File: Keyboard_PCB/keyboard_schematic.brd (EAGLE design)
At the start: 460 x 121 mm, 230 parts

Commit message: Updated Schematic
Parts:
- removed 0, 1, 2, 3, 4, 5, 6, 7, 8, 9, A, ALT, ALT2, B, BACKSLASH, BACKSONG, BACKSPACE_1, C, CAPSLOCK, COMMA, CTRL, CTRL2, D, DASH, DELETE, DELETE2, DOWN, E, END, ENTER2, EQUAL, EQUAL2, ESC, F, F1, F10, F11, F12, F2, F3, F4, F5, F6, F7, F8, F9, G, GRAVE, H, HOME, I, INSERT, J, K, KP_1, KP_2, KP_3, KP_4, KP_5, KP_52, KP_6, KP_62, KP_7, KP_8, KP_9, KP_ASTERISK, KP_DASH, KP_DEL, KP_SLASH, L, LBRACKET, LEFT, M, MENU, N, NEXTSONG, NUMLOCK, O, P, PAUSE, PAUSEPLAY, PERIOD, PGDN, PGUP, PRTSC, Q, QUOTE, R, RANDSONG, RBRACKET, RIGHT, S, SCROLLLOCK, SEMICOLON, SLASH, T, TAB, U, UNDERSCORE, UP, V, VOLUMEUP, VOLUMNEDOWN, W, WIN, WIN2, X, Y, Z: KEYSWITCH-RGBLED-MX-1U-RGB, Keyboard:MX-1U-RGB
- removed BACKSPACE, ENTER, KP_0, SHIFT, SHIFT2: KEYSWITCH-RGBLED-MX-2U-RGB, Keyboard:MX-2U-RGB
- removed D0, D1, D2, D3, D4, D5, D6, D7, D8, D9, DA, DALT, DALT2, DB, DBACKSLASH, DBACKSONG, DBACKSPACE, DBACKSPACE_1, DC, DCAPSLOCK, DCOMMA, DCTRL, DCTRL2, DD, DDASH, DDELETE, DDELETE2, DDOWN, DE, DEND, DENTER, DENTER2, DEQUAL, DEQUAL2, DESC, DF, DF1, DF10, DF11, DF12, DF2, DF3, DF4, DF5, DF6, DF7, DF8, DF9, DG, DGRAVE, DH, DHOME, DI, DINSERT, DJ, DK, DKP_0, DKP_1, DKP_2, DKP_3, DKP_4, DKP_5, DKP_52, DKP_6, DKP_62, DKP_7, DKP_8, DKP_9, DKP_ASTERISK, DKP_DASH, DKP_DEL, DKP_SLASH, DL, DLBRACKET, DLEFT, DM, DMENU, DN, DNEXTSONG, DNUMLOCK, DO, DP, DPAUSE, DPAUSEPLAY, DPERIOD, DPGDN, DPGUP, DPRTSC, DQ, DQUOTE, DR, DRANDSONG, DRBRACKET, DRIGHT, DS, DSCROLLLOCK, DSEMICOLON, DSHIFT, DSHIFT2, DSLASH, DSPACE, DT, DTAB, DU, DUNDERSCORE, DUP, DV, DVOLUMEUP, DVOLUMNEDOWN, DW, DWIN, DWIN2, DX, DY, DZ: 1N4148, Components:DO-35
- removed SPACE: KEYSWITCH-RGBLED-MX-6.25U-RGB, Keyboard:MX-6.25U-RGB
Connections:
- removed net ROW1.5: DBACKSONG.C, DESC.C, DF1.C, DF10.C, DF11.C, DF12.C, DF2.C, DF3.C, DF4.C, DF5.C, DF6.C, DF7.C, DF8.C, DF9.C, DNEXTSONG.C, DPAUSE.C, DPAUSEPLAY.C, DPRTSC.C, DRANDSONG.C, DSCROLLLOCK.C, DVOLUMEUP.C, DVOLUMNEDOWN.C
- removed net ROW2.5: D0.C, D1.C, D2.C, D3.C, D4.C, D5.C, D6.C, D7.C, D8.C, D9.C, DBACKSPACE.C, DDASH.C, DEQUAL.C, DGRAVE.C, DHOME.C, DINSERT.C, DKP_ASTERISK.C, DKP_DASH.C, DKP_SLASH.C, DNUMLOCK.C, DPGUP.C, DUNDERSCORE.C
- removed net ROW3.5: DBACKSLASH.C, DDELETE.C, DE.C, DEND.C, DI.C, DKP_7.C, DKP_8.C, DKP_9.C, DLBRACKET.C, DO.C, DP.C, DPGDN.C, DQ.C, DR.C, DRBRACKET.C, DT.C, DTAB.C, DU.C, DW.C, DY.C
- removed net ROW4.5: DA.C, DCAPSLOCK.C, DD.C, DENTER.C, DF.C, DG.C, DH.C, DJ.C, DK.C, DKP_4.C, DKP_52.C, DKP_6.C, DKP_62.C, DL.C, DQUOTE.C, DS.C, DSEMICOLON.C
- removed net ROW5.5: DB.C, DC.C, DCOMMA.C, DKP_1.C, DKP_2.C, DKP_3.C, DM.C, DN.C, DPERIOD.C, DSHIFT.C, DSHIFT2.C, DSLASH.C, DUP.C, DV.C, DX.C, DZ.C
- removed net ROW6.5: DALT.C, DALT2.C, DBACKSPACE_1.C, DCTRL.C, DCTRL2.C, DDOWN.C, DKP_0.C, DKP_DEL.C, DLEFT.C, DMENU.C, DRIGHT.C, DSPACE.C, DWIN.C, DWIN2.C

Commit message: Final Revision on positioning
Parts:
- added 0, 1, 2, 3, 4, 5, 6, 7, 8, 9, A, ALT, ALT2, B, BACKSLASH, BACKSONG, BACKSPACE_1, C, CAPSLOCK, COMMA, CTRL, CTRL2, D, DASH, DELETE, DELETE2, DOWN, E, END, ENTER2, EQUAL, EQUAL2, ESC, F, F1, F10, F11, F12, F2, F3, F4, F5, F6, F7, F8, F9, G, GRAVE, H, HOME, I, INSERT, J, K, KP_1, KP_2, KP_3, KP_4, KP_5, KP_52, KP_6, KP_62, KP_7, KP_8, KP_9, KP_ASTERISK, KP_DASH, KP_DEL, KP_SLASH, L, LBRACKET, LEFT, M, MENU, N, NEXTSONG, NUMLOCK, O, P, PAUSE, PAUSEPLAY, PERIOD, PGDN, PGUP, PRTSC, Q, QUOTE, R, RANDSONG, RBRACKET, RIGHT, S, SCROLLLOCK, SEMICOLON, SLASH, T, TAB, U, UNDERSCORE, UP, V, VOLUMEUP, VOLUMNEDOWN, W, WIN, WIN2, X, Y, Z: KEYSWITCH-RGBSMDLED-ALPSMX-1U-SMDRGB, Keyboard:ALPSMX-1U-SMDRGB
- added BACKSPACE, ENTER, KP_0, SHIFT, SHIFT2: KEYSWITCH-RGBSMDLED-ALPSMX-2U-SMDRGB, Keyboard:ALPSMX-2U-SMDRGB
- added D0, D1, D2, D3, D4, D5, D6, D7, D8, D9, DA, DALT, DALT2, DB, DBACKSLASH, DBACKSONG, DBACKSPACE, DBACKSPACE_1, DC, DCAPSLOCK, DCOMMA, DCTRL, DCTRL2, DD, DDASH, DDELETE, DDELETE2, DDOWN, DE, DEND, DENTER, DENTER2, DEQUAL, DEQUAL2, DESC, DF, DF1, DF10, DF11, DF12, DF2, DF3, DF4, DF5, DF6, DF7, DF8, DF9, DG, DGRAVE, DH, DHOME, DI, DINSERT, DJ, DK, DKP_0, DKP_1, DKP_2, DKP_3, DKP_4, DKP_5, DKP_52, DKP_6, DKP_62, DKP_7, DKP_8, DKP_9, DKP_ASTERISK, DKP_DASH, DKP_DEL, DKP_SLASH, DL, DLBRACKET, DLEFT, DM, DMENU, DN, DNEXTSONG, DNUMLOCK, DO, DP, DPAUSE, DPAUSEPLAY, DPERIOD, DPGDN, DPGUP, DPRTSC, DQ, DQUOTE, DR, DRANDSONG, DRBRACKET, DRIGHT, DS, DSCROLLLOCK, DSEMICOLON, DSHIFT, DSHIFT2, DSLASH, DSPACE, DT, DTAB, DU, DUNDERSCORE, DUP, DV, DVOLUMEUP, DVOLUMNEDOWN, DW, DWIN, DWIN2, DX, DY, DZ: (no value), Components:SOD-123
- added SPACE: KEYSWITCH-RGBSMDLED-ALPSMX-6.25U-SMDRGB, Keyboard:ALPSMX-6.25U-SMDRGB
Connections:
- new net N$1: DESC.A, ESC.ALPS2, ESC.MX2
- new net N$10: DF9.A, F9.ALPS2, F9.MX2
- new net N$100: DENTER2.A, ENTER2.ALPS2, ENTER2.MX2
- new net N$101: DDELETE2.A, DELETE2.ALPS2, DELETE2.MX2
- new net N$102: CTRL.ALPS2, CTRL.MX2, DCTRL.A
- new net N$103: DWIN.A, WIN.ALPS2, WIN.MX2
- new net N$104: ALT.ALPS2, ALT.MX2, DALT.A
- new net N$105: DSPACE.A, SPACE.ALPS2, SPACE.MX2
- new net N$106: ALT2.ALPS2, ALT2.MX2, DALT2.A
- new net N$107: DWIN2.A, WIN2.ALPS2, WIN2.MX2
- new net N$108: DMENU.A, MENU.ALPS2, MENU.MX2
- new net N$109: CTRL2.ALPS2, CTRL2.MX2, DCTRL2.A
- new net N$11: DF10.A, F10.ALPS2, F10.MX2
- new net N$110: DLEFT.A, LEFT.ALPS2, LEFT.MX2
- new net N$111: DDOWN.A, DOWN.ALPS2, DOWN.MX2
- new net N$112: DRIGHT.A, RIGHT.ALPS2, RIGHT.MX2
- new net N$113: DKP_0.A, KP_0.ALPS2, KP_0.MX2
- new net N$114: DKP_DEL.A, KP_DEL.ALPS2, KP_DEL.MX2
- new net N$115: BACKSPACE_1.ALPS2, BACKSPACE_1.MX2, DBACKSPACE_1.A
- new net N$12: DF11.A, F11.ALPS2, F11.MX2
- new net N$13: DF12.A, F12.ALPS2, F12.MX2
- new net N$14: DVOLUMEUP.A, VOLUMEUP.ALPS2, VOLUMEUP.MX2
- new net N$15: DVOLUMNEDOWN.A, VOLUMNEDOWN.ALPS2, VOLUMNEDOWN.MX2
- new net N$16: DPRTSC.A, PRTSC.ALPS2, PRTSC.MX2
- new net N$17: DSCROLLLOCK.A, SCROLLLOCK.ALPS2, SCROLLLOCK.MX2
- new net N$18: DPAUSE.A, PAUSE.ALPS2, PAUSE.MX2
- new net N$19: BACKSONG.ALPS2, BACKSONG.MX2, DBACKSONG.A
- new net N$2: DF1.A, F1.ALPS2, F1.MX2
- new net N$20: DPAUSEPLAY.A, PAUSEPLAY.ALPS2, PAUSEPLAY.MX2
- new net N$21: DNEXTSONG.A, NEXTSONG.ALPS2, NEXTSONG.MX2
- new net N$22: DRANDSONG.A, RANDSONG.ALPS2, RANDSONG.MX2
- new net N$23: DGRAVE.A, GRAVE.ALPS2, GRAVE.MX2
- new net N$24: 1.ALPS2, 1.MX2, D1.A
- new net N$25: 2.ALPS2, 2.MX2, D2.A
- new net N$26: 3.ALPS2, 3.MX2, D3.A
- new net N$27: 4.ALPS2, 4.MX2, D4.A
- new net N$28: 5.ALPS2, 5.MX2, D5.A
- new net N$29: 6.ALPS2, 6.MX2, D6.A
- new net N$3: DF2.A, F2.ALPS2, F2.MX2
- new net N$30: 7.ALPS2, 7.MX2, D7.A
- new net N$31: 8.ALPS2, 8.MX2, D8.A
- new net N$32: 9.ALPS2, 9.MX2, D9.A
- new net N$33: 0.ALPS2, 0.MX2, D0.A
- new net N$34: DASH.ALPS2, DASH.MX2, DDASH.A
- new net N$35: DEQUAL.A, EQUAL.ALPS2, EQUAL.MX2
- new net N$36: BACKSPACE.ALPS2, BACKSPACE.MX2, DBACKSPACE.A
- new net N$37: DINSERT.A, INSERT.ALPS2, INSERT.MX2
- new net N$38: DHOME.A, HOME.ALPS2, HOME.MX2
- new net N$39: DPGUP.A, PGUP.ALPS2, PGUP.MX2
- new net N$4: DF3.A, F3.ALPS2, F3.MX2
- new net N$40: DNUMLOCK.A, NUMLOCK.ALPS2, NUMLOCK.MX2
- new net N$41: DKP_SLASH.A, KP_SLASH.ALPS2, KP_SLASH.MX2
- new net N$42: DKP_ASTERISK.A, KP_ASTERISK.ALPS2, KP_ASTERISK.MX2
- new net N$43: DKP_DASH.A, KP_DASH.ALPS2, KP_DASH.MX2
- new net N$44: DUNDERSCORE.A, UNDERSCORE.ALPS2, UNDERSCORE.MX2
- new net N$45: DTAB.A, TAB.ALPS2, TAB.MX2
- new net N$46: DQ.A, Q.ALPS2, Q.MX2
- new net N$47: DW.A, W.ALPS2, W.MX2
- new net N$48: DE.A, E.ALPS2, E.MX2
- new net N$49: DR.A, R.ALPS2, R.MX2
- new net N$5: DF4.A, F4.ALPS2, F4.MX2
- new net N$50: DT.A, T.ALPS2, T.MX2
- new net N$51: DY.A, Y.ALPS2, Y.MX2
- new net N$52: DU.A, U.ALPS2, U.MX2
- new net N$53: DI.A, I.ALPS2, I.MX2
- new net N$54: DO.A, O.ALPS2, O.MX2
- new net N$55: DP.A, P.ALPS2, P.MX2
- new net N$56: DLBRACKET.A, LBRACKET.ALPS2, LBRACKET.MX2
- new net N$57: DRBRACKET.A, RBRACKET.ALPS2, RBRACKET.MX2
- new net N$58: BACKSLASH.ALPS2, BACKSLASH.MX2, DBACKSLASH.A
- new net N$59: DDELETE.A, DELETE.ALPS2, DELETE.MX2
- new net N$6: DF5.A, F5.ALPS2, F5.MX2
- new net N$60: DEND.A, END.ALPS2, END.MX2
- new net N$61: DPGDN.A, PGDN.ALPS2, PGDN.MX2
- new net N$62: DKP_7.A, KP_7.ALPS2, KP_7.MX2
- new net N$63: DKP_8.A, KP_8.ALPS2, KP_8.MX2
- new net N$64: DKP_9.A, KP_9.ALPS2, KP_9.MX2
- new net N$65: DEQUAL2.A, EQUAL2.ALPS2, EQUAL2.MX2
- new net N$66: DKP_5.A, KP_5.ALPS2, KP_5.MX2
- new net N$67: CAPSLOCK.ALPS2, CAPSLOCK.MX2, DCAPSLOCK.A
- new net N$68: A.ALPS2, A.MX2, DA.A
- new net N$69: DS.A, S.ALPS2, S.MX2
- new net N$7: DF6.A, F6.ALPS2, F6.MX2
- new net N$70: D.ALPS2, D.MX2, DD.A
- new net N$71: DF.A, F.ALPS2, F.MX2
- new net N$72: DG.A, G.ALPS2, G.MX2
- new net N$73: DH.A, H.ALPS2, H.MX2
- new net N$74: DJ.A, J.ALPS2, J.MX2
- new net N$75: DK.A, K.ALPS2, K.MX2
- new net N$76: DL.A, L.ALPS2, L.MX2
- new net N$77: DSEMICOLON.A, SEMICOLON.ALPS2, SEMICOLON.MX2
- new net N$78: DQUOTE.A, QUOTE.ALPS2, QUOTE.MX2
- new net N$79: DENTER.A, ENTER.ALPS2, ENTER.MX2
- new net N$8: DF7.A, F7.ALPS2, F7.MX2
- new net N$80: DKP_4.A, KP_4.ALPS2, KP_4.MX2
- new net N$81: DKP_52.A, KP_52.ALPS2, KP_52.MX2
- new net N$82: DKP_6.A, KP_6.ALPS2, KP_6.MX2
- new net N$83: DKP_62.A, KP_62.ALPS2, KP_62.MX2
- new net N$84: DSHIFT.A, SHIFT.ALPS2, SHIFT.MX2
- new net N$85: DZ.A, Z.ALPS2, Z.MX2
- new net N$86: DX.A, X.ALPS2, X.MX2
- new net N$87: C.ALPS2, C.MX2, DC.A
- new net N$88: DV.A, V.ALPS2, V.MX2
- new net N$89: B.ALPS2, B.MX2, DB.A
- new net N$9: DF8.A, F8.ALPS2, F8.MX2
- new net N$90: DN.A, N.ALPS2, N.MX2
- new net N$91: DM.A, M.ALPS2, M.MX2
- new net N$92: COMMA.ALPS2, COMMA.MX2, DCOMMA.A
- new net N$93: DPERIOD.A, PERIOD.ALPS2, PERIOD.MX2
- new net N$94: DSLASH.A, SLASH.ALPS2, SLASH.MX2
- new net N$95: DSHIFT2.A, SHIFT2.ALPS2, SHIFT2.MX2
- new net N$96: DUP.A, UP.ALPS2, UP.MX2
- new net N$97: DKP_1.A, KP_1.ALPS2, KP_1.MX2
- new net N$98: DKP_2.A, KP_2.ALPS2, KP_2.MX2
- new net N$99: DKP_3.A, KP_3.ALPS2, KP_3.MX2
- new net ROW1.5: DBACKSONG.C, DESC.C, DF1.C, DF10.C, DF11.C, DF12.C, DF2.C, DF3.C, DF4.C, DF5.C, DF6.C, DF7.C, DF8.C, DF9.C, DNEXTSONG.C, DPAUSE.C, DPAUSEPLAY.C, DPRTSC.C, DRANDSONG.C, DSCROLLLOCK.C, DVOLUMEUP.C, DVOLUMNEDOWN.C
- new net ROW2.5: D0.C, D1.C, D2.C, D3.C, D4.C, D5.C, D6.C, D7.C, D8.C, D9.C, DBACKSPACE.C, DDASH.C, DEQUAL.C, DGRAVE.C, DHOME.C, DINSERT.C, DKP_ASTERISK.C, DKP_DASH.C, DKP_SLASH.C, DNUMLOCK.C, DPGUP.C, DUNDERSCORE.C
- new net ROW3.5: DBACKSLASH.C, DDELETE.C, DE.C, DEND.C, DEQUAL2.C, DI.C, DKP_5.C, DKP_7.C, DKP_8.C, DKP_9.C, DLBRACKET.C, DO.C, DP.C, DPGDN.C, DQ.C, DR.C, DRBRACKET.C, DT.C, DTAB.C, DU.C, DW.C, DY.C
- new net ROW4.5: DA.C, DCAPSLOCK.C, DD.C, DENTER.C, DF.C, DG.C, DH.C, DJ.C, DK.C, DKP_4.C, DKP_52.C, DKP_6.C, DKP_62.C, DL.C, DQUOTE.C, DS.C, DSEMICOLON.C
- new net ROW5.5: DB.C, DC.C, DCOMMA.C, DDELETE2.C, DENTER2.C, DKP_1.C, DKP_2.C, DKP_3.C, DM.C, DN.C, DPERIOD.C, DSHIFT.C, DSHIFT2.C, DSLASH.C, DUP.C, DV.C, DX.C, DZ.C
- new net ROW6.5: DALT.C, DALT2.C, DBACKSPACE_1.C, DCTRL.C, DCTRL2.C, DDOWN.C, DKP_0.C, DKP_DEL.C, DLEFT.C, DMENU.C, DRIGHT.C, DSPACE.C, DWIN.C, DWIN2.C
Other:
- board size 460 x 121 mm -> 460 x 120 mm

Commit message: Fixed Board
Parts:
- removed DELETE2: KEYSWITCH-RGBSMDLED-ALPSMX-1U-SMDRGB, Keyboard:ALPSMX-1U-SMDRGB
- added KP_DELETE2: KEYSWITCH-RGBSMDLED-ALPSMX-1U-SMDRGB, Keyboard:ALPSMX-1U-SMDRGB
- moved DESC 117.4 mm to (14.6, 112.8), turned to 90 degrees
- moved DB 13.6 mm to (133.7, 36.6), turned to 90 degrees
- moved DC 13.6 mm to (95.6, 36.6), turned to 90 degrees
- moved DCOMMA 13.6 mm to (190.8, 36.6), turned to 90 degrees
- moved DDELETE2 13.6 mm to (443.3, 36.6), turned to 90 degrees
- moved DKP_1 13.6 mm to (367.1, 36.6), turned to 90 degrees
- moved DKP_2 13.6 mm to (386.1, 36.6), turned to 90 degrees
- moved DKP_3 13.6 mm to (405.2, 36.6), turned to 90 degrees
- moved DM 13.6 mm to (171.8, 36.6), turned to 90 degrees
- moved DN 13.6 mm to (152.7, 36.6), turned to 90 degrees
- moved DPERIOD 13.6 mm to (209.9, 36.6), turned to 90 degrees
- moved DSHIFT 13.6 mm to (26.5, 36.6), turned to 90 degrees
- moved DSHIFT2 13.6 mm to (264.7, 36.6), turned to 90 degrees
- moved DSLASH 13.6 mm to (228.9, 36.6), turned to 90 degrees
- moved DUP 13.6 mm to (324.2, 36.6), turned to 90 degrees
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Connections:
- net N$101: now also KP_DELETE2.ALPS2, KP_DELETE2.MX2; no longer DELETE2.ALPS2, DELETE2.MX2
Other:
- board size 460 x 120 mm -> 450 x 121 mm

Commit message: Updated alot and am having fun
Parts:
- removed DRANDSONG: (no value), Components:SOD-123
- added C1, C2: 22pF, rcl:C0805
- added C3, C4, C5, C6, C7: 0.1uF, rcl:C0805
- added C8: 1u, rcl:C0805
- added DLOCK, DM1, DM2, DM3, DM4, DM5, DM6, DNEXTSONG1: (no value), Components:SOD-123
- added J1: (no value), SparkFun-Connectors:USB-B-MICRO-SMD
- added LOCK, M6: KEYSWITCH-RGBSMDLED-ALPSMX-1U-SMDRGB, Keyboard:ALPSMX-1U-SMDRGB
- added M1, M2, M3, M4, M5: KEYSWITCH-RGBSMDLED-MX-1U-SMDRGB, Keyboard:MX-1U-SMDRGB
- added R1, R2: 10k, rcl:M0805
- added R3, R4: 22, rcl:M0805
- added S1: (no value), switch-omron:B3F-31XX
- added U$1: 32U4, SparkFun-IC-Microcontroller:TQFP44
- added Y1: (no value), SparkFun-Clocks:CRYSTAL-SMD-3.2X2.5MM
- moved D 22.1 mm to (77.0, 48.8), turned to 0 degrees
- moved DELETE 21.4 mm to (297.0, 67.8), turned to 0 degrees
- moved DOWN 21.4 mm to (316.1, 10.7), turned to 0 degrees
- moved DASH 21.0 mm to (216.1, 87.5), turned to 0 degrees
- moved RANDSONG 0.90 mm to (417.0, 106.0)
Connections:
- removed net ROW1.5: DBACKSONG.C, DESC.C, DF1.C, DF10.C, DF11.C, DF12.C, DF2.C, DF3.C, DF4.C, DF5.C, DF6.C, DF7.C, DF8.C, DF9.C, DNEXTSONG.C, DPAUSE.C, DPAUSEPLAY.C, DPRTSC.C, DRANDSONG.C, DSCROLLLOCK.C, DVOLUMEUP.C, DVOLUMNEDOWN.C
- removed net ROW2.5: D0.C, D1.C, D2.C, D3.C, D4.C, D5.C, D6.C, D7.C, D8.C, D9.C, DBACKSPACE.C, DDASH.C, DEQUAL.C, DGRAVE.C, DHOME.C, DINSERT.C, DKP_ASTERISK.C, DKP_DASH.C, DKP_SLASH.C, DNUMLOCK.C, DPGUP.C, DUNDERSCORE.C
- removed net ROW3.5: DBACKSLASH.C, DDELETE.C, DE.C, DEND.C, DEQUAL2.C, DI.C, DKP_5.C, DKP_7.C, DKP_8.C, DKP_9.C, DLBRACKET.C, DO.C, DP.C, DPGDN.C, DQ.C, DR.C, DRBRACKET.C, DT.C, DTAB.C, DU.C, DW.C, DY.C
- removed net ROW4.5: DA.C, DCAPSLOCK.C, DD.C, DENTER.C, DF.C, DG.C, DH.C, DJ.C, DK.C, DKP_4.C, DKP_52.C, DKP_6.C, DKP_62.C, DL.C, DQUOTE.C, DS.C, DSEMICOLON.C
- removed net ROW5.5: DB.C, DC.C, DCOMMA.C, DDELETE2.C, DENTER2.C, DKP_1.C, DKP_2.C, DKP_3.C, DM.C, DN.C, DPERIOD.C, DSHIFT.C, DSHIFT2.C, DSLASH.C, DUP.C, DV.C, DX.C, DZ.C
- removed net ROW6.5: DALT.C, DALT2.C, DBACKSPACE_1.C, DCTRL.C, DCTRL2.C, DDOWN.C, DKP_0.C, DKP_DEL.C, DLEFT.C, DMENU.C, DRIGHT.C, DSPACE.C, DWIN.C, DWIN2.C
- new net +5V: C3.1, C4.1, C5.1, C6.1, C7.1, J1.VBUS, R1.1, U$1.14, U$1.2, U$1.24, U$1.34, U$1.44
- new net GND: C1.2, C2.2, C3.2, C4.2, C5.2, C6.2, C7.2, C8.1, J1.GND, J1.SHIELD1, J1.SHIELD2, J1.SHIELD3, R2.1, S1.1, U$1.15, U$1.23, U$1.35, U$1.43, U$1.5
- new net N$116: C1.1, U$1.17, Y1.1
- new net N$117: C2.1, U$1.16, Y1.3
- new net N$118: R1.2, S1.2, U$1.13
- new net N$119: R2.2, U$1.33
- new net N$120: DM6.A, M6.ALPS2, M6.MX2
- new net N$121: J1.D+, R3.1
- new net N$122: J1.D-, R4.1
- new net N$123: R3.2, U$1.4
- new net N$124: R4.2, U$1.3
- new net N$125: C8.2, U$1.6
- new net N$126: DM1.A, M1.MX2
- new net N$127: DM2.A, M2.MX2
- new net N$128: DM3.A, M3.MX2
- new net N$129: DM4.A, M4.MX2
- new net N$130: DM5.A, M5.MX2
- new net N$131: DNEXTSONG1.A, RANDSONG.ALPS2, RANDSONG.MX2
- new net N$132: DF1.C, DF11.C, DF3.C, DF5.C, DF7.C, DF9.C, DM6.C, DNEXTSONG1.C, DPAUSE.C, DPAUSEPLAY.C, DPRTSC.C, DVOLUMEUP.C
- new net N$133: DBACKSONG.C, DESC.C, DF10.C, DF12.C, DF2.C, DF4.C, DF6.C, DF8.C, DLOCK.C, DNEXTSONG.C, DSCROLLLOCK.C, DVOLUMNEDOWN.C
- new net N$134: D1.C, D3.C, D5.C, D7.C, D9.C, DDASH.C, DINSERT.C, DKP_DASH.C, DKP_SLASH.C, DM5.C, DPGUP.C
- new net N$135: D0.C, D2.C, D4.C, D6.C, D8.C, DBACKSPACE.C, DEQUAL.C, DGRAVE.C, DHOME.C, DKP_ASTERISK.C, DNUMLOCK.C, DUNDERSCORE.C
- new net N$139: A.ALPS1, A.MX1
- new net N$140: MENU.ALPS1, MENU.MX1
- new net N$153: J.ALPS1, J.MX1
- new net N$154: KP_DELETE2.ALPS1, KP_DELETE2.MX1
- net N$22: now also DLOCK.A, LOCK.ALPS2, LOCK.MX2; no longer DRANDSONG.A, RANDSONG.ALPS2, RANDSONG.MX2
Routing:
- net GND: track 0.00 -> 88.8 mm
- net +5V: track 0.00 -> 38.8 mm
- net N$122: track 0.00 -> 11.1 mm
- net N$123: track 0.00 -> 10.4 mm
- net N$118: track 0.00 -> 6.33 mm
- net N$124: track 0.00 -> 5.91 mm
- net N$125: track 0.00 -> 5.66 mm
- net N$121: track 0.00 -> 5.53 mm
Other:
- board size 450 x 121 mm -> 589.5 x 222.5 mm

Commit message: Updated Schematic
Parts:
- removed M2, M3, M4, M5: KEYSWITCH-RGBSMDLED-MX-1U-SMDRGB, Keyboard:MX-1U-SMDRGB
- removed M6: KEYSWITCH-RGBSMDLED-ALPSMX-1U-SMDRGB, Keyboard:ALPSMX-1U-SMDRGB
- removed Y1: (no value), SparkFun-Clocks:CRYSTAL-SMD-3.2X2.5MM
- added CAPSLOCK1, ESC1, GRAVE1, TAB1: KEYSWITCH-RGBSMDLED-ALPSMX-1U-SMDRGB, Keyboard:ALPSMX-1U-SMDRGB
- added SHIFT1: KEYSWITCH-RGBSMDLED-ALPSMX-2U-SMDRGB, Keyboard:ALPSMX-2U-SMDRGB
- added Y2: CRYSTAL-GROUNDEDSMD-3.2X2.5, SparkFun-Clocks:CRYSTAL-SMD-3.2X2.5MM
- moved C2 50.7 mm to (394.6, 143.7), turned to 0 degrees
- moved C1 48.8 mm to (394.8, 137.8)
- moved R2 28.5 mm to (414.1, 135.6)
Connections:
- net +5V renamed VCC
- removed net N$126: DM1.A, M1.MX2
- removed net N$132: DF1.C, DF11.C, DF3.C, DF5.C, DF7.C, DF9.C, DM6.C, DNEXTSONG1.C, DPAUSE.C, DPAUSEPLAY.C, DPRTSC.C, DVOLUMEUP.C
- removed net N$133: DBACKSONG.C, DESC.C, DF10.C, DF12.C, DF2.C, DF4.C, DF6.C, DF8.C, DLOCK.C, DNEXTSONG.C, DSCROLLLOCK.C, DVOLUMNEDOWN.C
- removed net N$134: D1.C, D3.C, D5.C, D7.C, D9.C, DDASH.C, DINSERT.C, DKP_DASH.C, DKP_SLASH.C, DM5.C, DPGUP.C
- removed net N$135: D0.C, D2.C, D4.C, D6.C, D8.C, DBACKSPACE.C, DEQUAL.C, DGRAVE.C, DHOME.C, DKP_ASTERISK.C, DNUMLOCK.C, DUNDERSCORE.C
- removed net N$139: A.ALPS1, A.MX1
- removed net N$140: MENU.ALPS1, MENU.MX1
- removed net N$153: J.ALPS1, J.MX1
- removed net N$154: KP_DELETE2.ALPS1, KP_DELETE2.MX1
- new net COL1: CAPSLOCK.ALPS1, CAPSLOCK.MX1, CAPSLOCK1.ALPS1, CAPSLOCK1.MX1, ESC.ALPS1, ESC.MX1, ESC1.ALPS1, ESC1.MX1, GRAVE.ALPS1, GRAVE.MX1, GRAVE1.ALPS1, GRAVE1.MX1, M1.MX1, SHIFT.ALPS1, SHIFT.MX1, SHIFT1.ALPS1, SHIFT1.MX1, TAB.ALPS1, TAB.MX1, TAB1.ALPS1, TAB1.MX1, U$1.36
- new net COL10: BACKSONG.ALPS1, BACKSONG.MX1, ENTER2.ALPS1, ENTER2.MX1, KP_3.ALPS1, KP_3.MX1, KP_6.ALPS1, KP_6.MX1, KP_7.ALPS1, KP_7.MX1, KP_8.ALPS1, KP_8.MX1, KP_DEL.ALPS1, KP_DEL.MX1, KP_SLASH.ALPS1, KP_SLASH.MX1, NUMLOCK.ALPS1, NUMLOCK.MX1, PAUSE.ALPS1, PAUSE.MX1, U$1.31
- new net COL11: EQUAL2.ALPS1, EQUAL2.MX1, KP_9.ALPS1, KP_9.MX1, KP_ASTERISK.ALPS1, KP_ASTERISK.MX1, KP_DASH.ALPS1, KP_DASH.MX1, NEXTSONG.ALPS1, NEXTSONG.MX1, PAUSEPLAY.ALPS1, PAUSEPLAY.MX1, U$1.27
- new net COL12: BACKSPACE_1.ALPS1, BACKSPACE_1.MX1, KP_5.ALPS1, KP_5.MX1, KP_62.ALPS1, KP_62.MX1, KP_DELETE2.ALPS1, KP_DELETE2.MX1, LOCK.ALPS1, LOCK.MX1, RANDSONG.ALPS1, RANDSONG.MX1, U$1.1, UNDERSCORE.ALPS1, UNDERSCORE.MX1
- new net COL2: 1.ALPS1, 1.MX1, 2.ALPS1, 2.MX1, A.ALPS1, A.MX1, CTRL.ALPS1, CTRL.MX1, F1.ALPS1, F1.MX1, F2.ALPS1, F2.MX1, Q.ALPS1, Q.MX1, S.ALPS1, S.MX1, U$1.37, W.ALPS1, W.MX1, X.ALPS1, X.MX1, Z.ALPS1, Z.MX1
- new net COL3: 3.ALPS1, 3.MX1, 4.ALPS1, 4.MX1, C.ALPS1, C.MX1, D.ALPS1, D.MX1, E.ALPS1, E.MX1, F.ALPS1, F.MX1, F3.ALPS1, F3.MX1, F4.ALPS1, F4.MX1, R.ALPS1, R.MX1, U$1.38, V.ALPS1, V.MX1, WIN.ALPS1, WIN.MX1
- new net COL4: 5.ALPS1, 5.MX1, 6.ALPS1, 6.MX1, ALT.ALPS1, ALT.MX1, B.ALPS1, B.MX1, F5.ALPS1, F5.MX1, F6.ALPS1, F6.MX1, G.ALPS1, G.MX1, H.ALPS1, H.MX1, N.ALPS1, N.MX1, T.ALPS1, T.MX1, U$1.39, Y.ALPS1, Y.MX1
- new net COL5: 7.ALPS1, 7.MX1, 8.ALPS1, 8.MX1, COMMA.ALPS1, COMMA.MX1, F7.ALPS1, F7.MX1, F8.ALPS1, F8.MX1, I.ALPS1, I.MX1, J.ALPS1, J.MX1, K.ALPS1, K.MX1, M.ALPS1, M.MX1, SPACE.ALPS1, SPACE.MX1, U$1.40, U.ALPS1, U.MX1
- new net COL6: 0.ALPS1, 0.MX1, 9.ALPS1, 9.MX1, ALT2.ALPS1, ALT2.MX1, F10.ALPS1, F10.MX1, F9.ALPS1, F9.MX1, L.ALPS1, L.MX1, O.ALPS1, O.MX1, P.ALPS1, P.MX1, PERIOD.ALPS1, PERIOD.MX1, SEMICOLON.ALPS1, SEMICOLON.MX1, SLASH.ALPS1, SLASH.MX1, U$1.41
- new net COL7: DASH.ALPS1, DASH.MX1, ENTER.ALPS1, ENTER.MX1, EQUAL.ALPS1, EQUAL.MX1, F11.ALPS1, F11.MX1, F12.ALPS1, F12.MX1, LBRACKET.ALPS1, LBRACKET.MX1, MENU.ALPS1, MENU.MX1, QUOTE.ALPS1, QUOTE.MX1, RBRACKET.ALPS1, RBRACKET.MX1, SHIFT2.ALPS1, SHIFT2.MX1, U$1.19, WIN2.ALPS1, WIN2.MX1
- new net COL8: BACKSLASH.ALPS1, BACKSLASH.MX1, BACKSPACE.ALPS1, BACKSPACE.MX1, CTRL2.ALPS1, CTRL2.MX1, DELETE.ALPS1, DELETE.MX1, DOWN.ALPS1, DOWN.MX1, INSERT.ALPS1, INSERT.MX1, LEFT.ALPS1, LEFT.MX1, RIGHT.ALPS1, RIGHT.MX1, U$1.18, UP.ALPS1, UP.MX1, VOLUMEUP.ALPS1, VOLUMEUP.MX1, VOLUMNEDOWN.ALPS1, VOLUMNEDOWN.MX1
- new net COL9: END.ALPS1, END.MX1, HOME.ALPS1, HOME.MX1, KP_0.ALPS1, KP_0.MX1, KP_1.ALPS1, KP_1.MX1, KP_2.ALPS1, KP_2.MX1, KP_4.ALPS1, KP_4.MX1, KP_52.ALPS1, KP_52.MX1, PGDN.ALPS1, PGDN.MX1, PGUP.ALPS1, PGUP.MX1, PRTSC.ALPS1, PRTSC.MX1, SCROLLLOCK.ALPS1, SCROLLLOCK.MX1, U$1.25
- new net ROW1.1: DF1.C, DF11.C, DF3.C, DF5.C, DF7.C, DF9.C, DM6.C, DNEXTSONG1.C, DPAUSE.C, DPAUSEPLAY.C, DSCROLLLOCK.C, DVOLUMEUP.C, U$1.28
- new net ROW1.2: DBACKSONG.C, DESC.C, DF10.C, DF12.C, DF2.C, DF4.C, DF6.C, DF8.C, DLOCK.C, DNEXTSONG.C, DPRTSC.C, DVOLUMNEDOWN.C, U$1.29
- new net ROW2.1: D1.C, D3.C, D5.C, D7.C, D9.C, DBACKSPACE.C, DDASH.C, DHOME.C, DKP_DASH.C, DKP_SLASH.C, DM5.C, U$1.30
- new net ROW2.2: D0.C, D2.C, D4.C, D6.C, D8.C, DEQUAL.C, DGRAVE.C, DINSERT.C, DKP_ASTERISK.C, DNUMLOCK.C, DPGUP.C, DUNDERSCORE.C, U$1.12
- new net ROW3.1: DBACKSLASH.C, DE.C, DEND.C, DEQUAL2.C, DKP_8.C, DLBRACKET.C, DM4.C, DO.C, DQ.C, DT.C, DU.C, U$1.26
- new net ROW3.2: DDELETE.C, DI.C, DKP_5.C, DKP_7.C, DKP_9.C, DP.C, DPGDN.C, DR.C, DRBRACKET.C, DTAB.C, DW.C, DY.C, U$1.32
- new net ROW4.1: DA.C, DCTRL2.C, DD.C, DG.C, DJ.C, DKP_4.C, DKP_6.C, DKP_62.C, DL.C, DM3.C, DQUOTE.C, U$1.8
- new net ROW4.2: DCAPSLOCK.C, DENTER.C, DENTER2.C, DF.C, DH.C, DK.C, DKP_52.C, DS.C, DSEMICOLON.C, DUP.C, U$1.9
- new net ROW5.1: DB.C, DC.C, DKP_2.C, DLEFT.C, DM.C, DM2.C, DMENU.C, DPERIOD.C, DZ.C, U$1.10
- new net ROW5.2: DCOMMA.C, DDELETE2.C, DKP_1.C, DKP_3.C, DN.C, DRIGHT.C, DSHIFT.C, DSHIFT2.C, DSLASH.C, DV.C, DX.C, U$1.11
- new net ROW6.1: DALT.C, DALT2.C, DBACKSPACE_1.C, DCTRL.C, DDOWN.C, DKP_0.C, DKP_DEL.C, DM1.C, DSPACE.C, DWIN.C, DWIN2.C, U$1.22
- net GND: now also Y2.2, Y2.4
- net N$116: now also Y2.1; no longer Y1.1
- net N$117: now also Y2.3; no longer Y1.3
- net N$120: now also ESC1.ALPS2, ESC1.MX2; no longer M6.ALPS2, M6.MX2
- net N$127: now also DM5.A, GRAVE1.ALPS2, GRAVE1.MX2; no longer DM2.A, M2.MX2
- net N$128: now also DM4.A, TAB1.ALPS2, TAB1.MX2; no longer DM3.A, M3.MX2
- net N$129: now also CAPSLOCK1.ALPS2, CAPSLOCK1.MX2, DM3.A; no longer DM4.A, M4.MX2
- net N$130: now also DM2.A, SHIFT1.ALPS2, SHIFT1.MX2; no longer DM5.A, M5.MX2
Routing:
- net VCC: track 38.8 -> 81.7 mm, vias 0 -> 3
- net GND: track 88.8 -> 112.7 mm
- net N$118: track 6.33 -> 26.7 mm
- net N$117: track 0.00 -> 10.5 mm
- net N$116: track 0.00 -> 9.23 mm
- net N$119: track 0.00 -> 1.65 mm

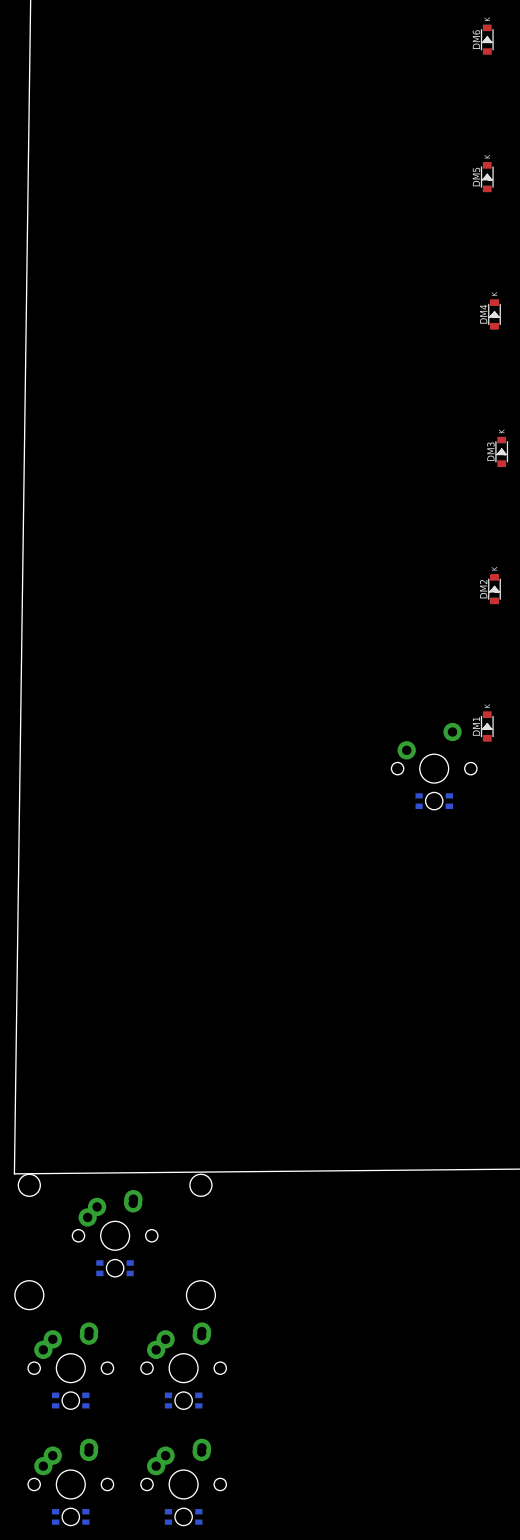
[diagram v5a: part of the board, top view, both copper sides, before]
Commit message: Fixed Keys and added boardpng
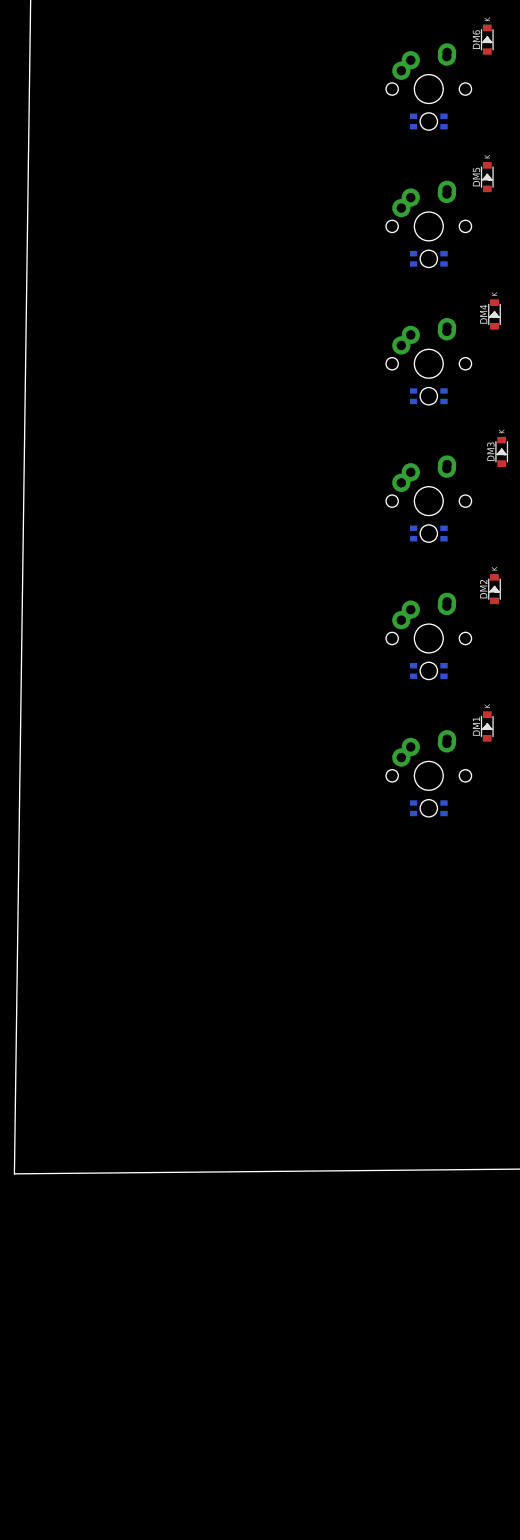
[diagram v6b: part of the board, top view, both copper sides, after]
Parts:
- removed CAPSLOCK1, ESC1, GRAVE1, TAB1: KEYSWITCH-RGBSMDLED-ALPSMX-1U-SMDRGB, Keyboard:ALPSMX-1U-SMDRGB
- removed M1: KEYSWITCH-RGBSMDLED-MX-1U-SMDRGB, Keyboard:MX-1U-SMDRGB
- removed SHIFT1: KEYSWITCH-RGBSMDLED-ALPSMX-2U-SMDRGB, Keyboard:ALPSMX-2U-SMDRGB
- added CTRL1, M2, M3, M4, M5, M6: KEYSWITCH-RGBSMDLED-ALPSMX-1U-SMDRGB, Keyboard:ALPSMX-1U-SMDRGB
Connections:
- new net N$126: DM2.A, M2.ALPS2, M2.MX2
- net COL1: now also CTRL1.ALPS1, CTRL1.MX1, M2.ALPS1, M2.MX1, M3.ALPS1, M3.MX1, M4.ALPS1, M4.MX1, M5.ALPS1, M5.MX1, M6.ALPS1, M6.MX1; no longer CAPSLOCK1.ALPS1, CAPSLOCK1.MX1, ESC1.ALPS1, ESC1.MX1, GRAVE1.ALPS1, GRAVE1.MX1, M1.MX1, SHIFT1.ALPS1, SHIFT1.MX1, TAB1.ALPS1, TAB1.MX1
- net N$120: now also M6.ALPS2, M6.MX2; no longer ESC1.ALPS2, ESC1.MX2
- net N$127: now also M5.ALPS2, M5.MX2; no longer GRAVE1.ALPS2, GRAVE1.MX2
- net N$128: now also M4.ALPS2, M4.MX2; no longer TAB1.ALPS2, TAB1.MX2
- net N$129: now also M3.ALPS2, M3.MX2; no longer CAPSLOCK1.ALPS2, CAPSLOCK1.MX2
- net N$130: now also CTRL1.ALPS2, CTRL1.MX2, DM1.A; no longer DM2.A, SHIFT1.ALPS2, SHIFT1.MX2
